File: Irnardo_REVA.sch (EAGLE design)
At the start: 21 parts, among them U1 ATMEGA32U4-MU, U2 TSOP755, X1 16MHz

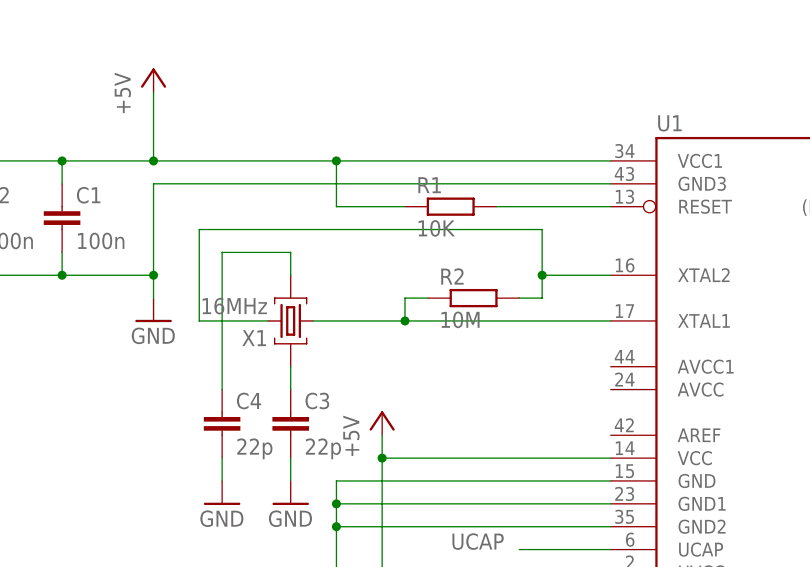
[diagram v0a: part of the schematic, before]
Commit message: Initial PCB design for DIY etching - incomplete
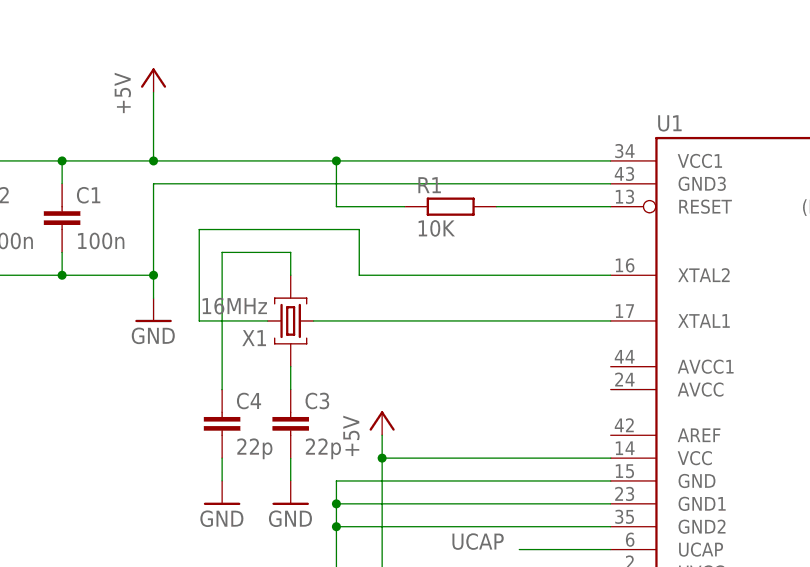
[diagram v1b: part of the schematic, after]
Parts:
- removed R2: 10M, resistor:R-EU_R0402
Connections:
- net N$1: no longer R2.1
- net N$2: no longer R2.2
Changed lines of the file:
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@@
 <?xml version="1.0" encoding="utf-8"?>
 <!DOCTYPE eagle SYSTEM "eagle.dtd">
-<eagle version="6.5.0">
+<eagle version="6.4">
 <drawing>
 <settings>
@@
 <part name="R1" library="resistor" deviceset="R-EU_" device="R0402" value="10K"/>
 <part name="C1" library="resistor" deviceset="C-EU" device="C0402" value="100n"/>
-<part name="R2" library="resistor" deviceset="R-EU_" device="R0402" value="10M"/>
 <part name="P+3" library="supply1" deviceset="+5V" device=""/>
 <part name="GND3" library="supply1" deviceset="GND" device=""/>
@@
 <instance part="R1" gate="G$1" x="58.42" y="101.6"/>
 <instance part="C1" gate="G$1" x="15.24" y="101.6"/>
-<instance part="R2" gate="G$1" x="60.96" y="91.44"/>
 <instance part="P+3" gate="1" x="50.8" y="78.74"/>
 <instance part="GND3" gate="1" x="45.72" y="55.88"/>
@@
 <pinref part="U1" gate="G$1" pin="XTAL1"/>
 <pinref part="X1" gate="G$1" pin="C1"/>
-<wire x1="76.2" y1="88.9" x2="53.34" y2="88.9" width="0.1524" layer="91"/>
-<pinref part="R2" gate="G$1" pin="1"/>
-<wire x1="53.34" y1="88.9" x2="43.18" y2="88.9" width="0.1524" layer="91"/>
-<wire x1="55.88" y1="91.44" x2="53.34" y2="91.44" width="0.1524" layer="91"/>
-<wire x1="53.34" y1="91.44" x2="53.34" y2="88.9" width="0.1524" layer="91"/>
-<junction x="53.34" y="88.9"/>
+<wire x1="76.2" y1="88.9" x2="43.18" y2="88.9" width="0.1524" layer="91"/>
 </segment>
 </net>
@@
 <segment>
 <pinref part="U1" gate="G$1" pin="XTAL2"/>
-<wire x1="76.2" y1="93.98" x2="68.58" y2="93.98" width="0.1524" layer="91"/>
-<wire x1="68.58" y1="93.98" x2="68.58" y2="99.06" width="0.1524" layer="91"/>
-<wire x1="68.58" y1="99.06" x2="30.48" y2="99.06" width="0.1524" layer="91"/>
+<wire x1="76.2" y1="93.98" x2="48.26" y2="93.98" width="0.1524" layer="91"/>
+<wire x1="48.26" y1="93.98" x2="48.26" y2="99.06" width="0.1524" layer="91"/>
+<wire x1="48.26" y1="99.06" x2="30.48" y2="99.06" width="0.1524" layer="91"/>
 <wire x1="30.48" y1="99.06" x2="30.48" y2="88.9" width="0.1524" layer="91"/>
 <pinref part="X1" gate="G$1" pin="C2"/>
 <wire x1="30.48" y1="88.9" x2="38.1" y2="88.9" width="0.1524" layer="91"/>
-<pinref part="R2" gate="G$1" pin="2"/>
-<wire x1="66.04" y1="91.44" x2="68.58" y2="91.44" width="0.1524" layer="91"/>
-<wire x1="68.58" y1="91.44" x2="68.58" y2="93.98" width="0.1524" layer="91"/>
-<junction x="68.58" y="93.98"/>
-</segment>
-</net>
+</segment>
+</net>

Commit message: Finished placing and stated wiring REVA
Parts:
- added J1: ICSP, 6X2005IN:6X2005IN
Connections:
- removed net N$3: R1.2, U1.RESET
- removed net N$4: C4.1, X1.GND@1
- removed net N$6: C3.1, X1.GND@2
- new net MISO: J1.1, U1.(PD0/MISO/PCINT3)PB3
- new net MOSI: J1.4, U1.(PDI/MOSI/PCINT2)PB2
- new net RESET: J1.5, R1.2, U1.RESET
- new net SCK: J1.3, U1.(SCLK/PCINT1)PB1
- net +5V: now also J1.2
- net GND: now also J1.6, X1.GND@1, X1.GND@2
- net N$1: now also C3.1
- net N$2: now also C4.1
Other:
- note added: "ICSP"
- note added: "REVA"
- note added: "© 2014 - Bracken Dawson"
- moved on the sheet: C3, C4, R1, X1
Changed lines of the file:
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@@
 <?xml version="1.0" encoding="utf-8"?>
 <!DOCTYPE eagle SYSTEM "eagle.dtd">
-<eagle version="6.4">
+<eagle version="6.5.0">
 <drawing>
 <settings>
@@
 <part name="C7" library="resistor" deviceset="C-EU" device="C0402" value="100n"/>
 <part name="GND12" library="supply1" deviceset="GND" device=""/>
+<part name="P+5" library="supply1" deviceset="+5V" device=""/>
+<part name="GND13" library="supply1" deviceset="GND" device=""/>
+<part name="J1" library="6X2005IN" deviceset="6X2005IN" device="" value="ICSP"/>
 </parts>
 <sheets>
@@
 <frame x1="-48.26" y1="-20.32" x2="256.54" y2="172.72" columns="8" rows="5" layer="91"/>
 <text x="155.194" y="74.93" size="1.778" layer="97">USB Boot En</text>
+<text x="-33.02" y="132.08" size="5.08" layer="91">REVA</text>
+<text x="167.64" y="-12.7" size="5.08" layer="91">© 2014 - Bracken Dawson</text>
+<text x="175.26" y="40.64" size="5.08" layer="91">ICSP</text>
 </plain>
 <instances>
@@
 <instance part="P+1" gate="1" x="25.4" y="116.84"/>
 <instance part="GND1" gate="1" x="25.4" y="88.9"/>
-<instance part="R1" gate="G$1" x="58.42" y="101.6"/>
+<instance part="R1" gate="G$1" x="58.42" y="109.22"/>
 <instance part="C1" gate="G$1" x="15.24" y="101.6"/>
 <instance part="P+3" gate="1" x="50.8" y="78.74"/>
 <instance part="GND3" gate="1" x="45.72" y="55.88"/>
 <instance part="GND4" gate="1" x="68.58" y="25.4"/>
-<instance part="X1" gate="G$1" x="40.64" y="88.9" rot="R180"/>
-<instance part="C3" gate="G$1" x="40.64" y="78.74"/>
-<instance part="C4" gate="G$1" x="33.02" y="78.74"/>
-<instance part="GND2" gate="1" x="40.64" y="68.58"/>
+<instance part="X1" gate="G$1" x="35.56" y="88.9" rot="R180"/>
+<instance part="C3" gate="G$1" x="40.64" y="83.82"/>
+<instance part="C4" gate="G$1" x="30.48" y="83.82"/>
+<instance part="GND2" gate="1" x="40.64" y="71.12"/>
 <instance part="C2" gate="G$1" x="5.08" y="101.6"/>
-<instance part="GND5" gate="1" x="33.02" y="68.58"/>
+<instance part="GND5" gate="1" x="30.48" y="71.12"/>
 <instance part="R3" gate="G$1" x="-12.7" y="45.72"/>
 <instance part="R4" gate="G$1" x="-12.7" y="38.1"/>
@@
 <instance part="C7" gate="G$1" x="10.16" y="53.34" rot="R90"/>
 <instance part="GND12" gate="1" x="22.86" y="53.34" rot="R90"/>
+<instance part="P+5" gate="1" x="215.9" y="38.1"/>
+<instance part="GND13" gate="1" x="215.9" y="12.7"/>
+<instance part="J1" gate="G$1" x="195.58" y="25.4"/>
 </instances>
 <busses>
@@
 <junction x="25.4" y="106.68"/>
 <pinref part="R1" gate="G$1" pin="1"/>
-<wire x1="53.34" y1="101.6" x2="45.72" y2="101.6" width="0.1524" layer="91"/>
-<wire x1="45.72" y1="101.6" x2="45.72" y2="106.68" width="0.1524" layer="91"/>
+<wire x1="53.34" y1="109.22" x2="45.72" y2="109.22" width="0.1524" layer="91"/>
+<wire x1="45.72" y1="109.22" x2="45.72" y2="106.68" width="0.1524" layer="91"/>
 <junction x="45.72" y="106.68"/>
 <pinref part="C2" gate="G$1" pin="1"/>
@@
 <wire x1="182.88" y1="93.98" x2="182.88" y2="96.52" width="0.1524" layer="91"/>
 <junction x="182.88" y="96.52"/>
+</segment>
+<segment>
+<pinref part="P+5" gate="1" pin="+5V"/>
+<wire x1="205.74" y1="27.94" x2="215.9" y2="27.94" width="0.1524" layer="91"/>
+<wire x1="215.9" y1="27.94" x2="215.9" y2="35.56" width="0.1524" layer="91"/>
+<pinref part="J1" gate="G$1" pin="2"/>
 </segment>
 </net>
@@
 <pinref part="GND2" gate="1" pin="GND"/>
 <pinref part="C3" gate="G$1" pin="2"/>
-<wire x1="40.64" y1="73.66" x2="40.64" y2="71.12" width="0.1524" layer="91"/>
+<wire x1="40.64" y1="78.74" x2="40.64" y2="76.2" width="0.1524" layer="91"/>
+<pinref part="X1" gate="G$1" pin="GND@2"/>
+<wire x1="40.64" y1="76.2" x2="40.64" y2="73.66" width="0.1524" layer="91"/>
+<wire x1="35.56" y1="83.82" x2="35.56" y2="76.2" width="0.1524" layer="91"/>
+<wire x1="35.56" y1="76.2" x2="40.64" y2="76.2" width="0.1524" layer="91"/>
+<wire x1="40.64" y1="76.2" x2="45.72" y2="76.2" width="0.1524" layer="91"/>
+<wire x1="45.72" y1="76.2" x2="45.72" y2="96.52" width="0.1524" layer="91"/>
+<wire x1="45.72" y1="96.52" x2="35.56" y2="96.52" width="0.1524" layer="91"/>
+<pinref part="X1" gate="G$1" pin="GND@1"/>
+<wire x1="35.56" y1="96.52" x2="35.56" y2="93.98" width="0.1524" layer="91"/>
+<junction x="40.64" y="76.2"/>
 </segment>
 <segment>
 <pinref part="C4" gate="G$1" pin="2"/>
-<wire x1="33.02" y1="73.66" x2="33.02" y2="71.12" width="0.1524" layer="91"/>
+<wire x1="30.48" y1="78.74" x2="30.48" y2="73.66" width="0.1524" layer="91"/>
 <pinref part="GND5" gate="1" pin="GND"/>
 </segment>
@@
 <wire x1="15.24" y1="53.34" x2="20.32" y2="53.34" width="0.1524" layer="91"/>
 </segment>
-</net>
-<net name="N$3" class="0">
+<segment>
+<wire x1="205.74" y1="22.86" x2="215.9" y2="22.86" width="0.1524" layer="91"/>
+<pinref part="GND13" gate="1" pin="GND"/>
+<wire x1="215.9" y1="22.86" x2="215.9" y2="15.24" width="0.1524" layer="91"/>
+<pinref part="J1" gate="G$1" pin="6"/>
+</segment>
+</net>
+<net name="RESET" class="0">
 <segment>
 <pinref part="U1" gate="G$1" pin="RESET"/>
 <pinref part="R1" gate="G$1" pin="2"/>
-<wire x1="76.2" y1="101.6" x2="63.5" y2="101.6" width="0.1524" layer="91"/>
+<wire x1="76.2" y1="101.6" x2="71.12" y2="101.6" width="0.1524" layer="91"/>
+<wire x1="71.12" y1="101.6" x2="71.12" y2="109.22" width="0.1524" layer="91"/>
+<wire x1="71.12" y1="109.22" x2="63.5" y2="109.22" width="0.1524" layer="91"/>
+<wire x1="71.12" y1="101.6" x2="66.04" y2="101.6" width="0.1524" layer="91"/>
+<junction x="71.12" y="101.6"/>
+<label x="55.88" y="101.6" size="1.778" layer="95"/>
+</segment>
+<segment>
+<wire x1="185.42" y1="22.86" x2="175.26" y2="22.86" width="0.1524" layer="91"/>
+<label x="165.1" y="22.86" size="1.778" layer="95"/>
+<pinref part="J1" gate="G$1" pin="5"/>
 </segment>
 </net>
@@
 <pinref part="U1" gate="G$1" pin="XTAL1"/>
 <pinref part="X1" gate="G$1" pin="C1"/>
-<wire x1="76.2" y1="88.9" x2="43.18" y2="88.9" width="0.1524" layer="91"/>
+<wire x1="76.2" y1="88.9" x2="40.64" y2="88.9" width="0.1524" layer="91"/>
+<pinref part="C3" gate="G$1" pin="1"/>
+<wire x1="40.64" y1="88.9" x2="38.1" y2="88.9" width="0.1524" layer="91"/>
+<wire x1="40.64" y1="86.36" x2="40.64" y2="88.9" width="0.1524" layer="91"/>
+<junction x="40.64" y="88.9"/>
 </segment>
 </net>
@@
 <wire x1="30.48" y1="99.06" x2="30.48" y2="88.9" width="0.1524" layer="91"/>
 <pinref part="X1" gate="G$1" pin="C2"/>
-<wire x1="30.48" y1="88.9" x2="38.1" y2="88.9" width="0.1524" layer="91"/>
-</segment>
-</net>
-<net name="N$4" class="0">
-<segment>
-<pinref part="X1" gate="G$1" pin="GND@1"/>
-<wire x1="40.64" y1="93.98" x2="40.64" y2="96.52" width="0.1524" layer="91"/>
-<wire x1="40.64" y1="96.52" x2="33.02" y2="96.52" width="0.1524" layer="91"/>
 <pinref part="C4" gate="G$1" pin="1"/>
-<wire x1="33.02" y1="96.52" x2="33.02" y2="81.28" width="0.1524" layer="91"/>
-</segment>
-</net>
-<net name="N$6" class="0">
-<segment>
-<pinref part="C3" gate="G$1" pin="1"/>
-<pinref part="X1" gate="G$1" pin="GND@2"/>
-<wire x1="40.64" y1="81.28" x2="40.64" y2="83.82" width="0.1524" layer="91"/>
+<wire x1="30.48" y1="88.9" x2="33.02" y2="88.9" width="0.1524" layer="91"/>
+<wire x1="30.48" y1="86.36" x2="30.48" y2="88.9" width="0.1524" layer="91"/>
+<junction x="30.48" y="88.9"/>
 </segment>
 </net>
@@
 </segment>
 </net>
+<net name="MISO" class="0">
+<segment>
+<pinref part="U1" gate="G$1" pin="(PD0/MISO/PCINT3)PB3"/>
+<wire x1="137.16" y1="96.52" x2="147.32" y2="96.52" width="0.1524" layer="91"/>
+<label x="147.32" y="96.52" size="1.778" layer="95"/>
+</segment>
+<segment>
+<wire x1="185.42" y1="27.94" x2="175.26" y2="27.94" width="0.1524" layer="91"/>
+<label x="167.64" y="27.94" size="1.778" layer="95"/>
+<pinref part="J1" gate="G$1" pin="1"/>
+</segment>
+</net>
+<net name="SCK" class="0">
+<segment>
+<pinref part="U1" gate="G$1" pin="(SCLK/PCINT1)PB1"/>
+<wire x1="137.16" y1="91.44" x2="147.32" y2="91.44" width="0.1524" layer="91"/>
+<label x="147.32" y="91.44" size="1.778" layer="95"/>
+</segment>
+<segment>
+<wire x1="185.42" y1="25.4" x2="175.26" y2="25.4" width="0.1524" layer="91"/>
+<label x="167.64" y="25.4" size="1.778" layer="95"/>
+<pinref part="J1" gate="G$1" pin="3"/>
+</segment>
+</net>
+<net name="MOSI" class="0">
+<segment>
+<pinref part="U1" gate="G$1" pin="(PDI/MOSI/PCINT2)PB2"/>
+<wire x1="137.16" y1="93.98" x2="147.32" y2="93.98" width="0.1524" layer="91"/>
+<label x="147.32" y="93.98" size="1.778" layer="95"/>
+</segment>
+<segment>
+<wire x1="205.74" y1="25.4" x2="215.9" y2="25.4" width="0.1524" layer="91"/>
+<label x="215.9" y="25.4" size="1.778" layer="95"/>
+<pinref part="J1" gate="G$1" pin="4"/>
+</segment>
+</net>

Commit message: First complete(ish) layout.
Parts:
- removed R8: 10K, resistor:R-EU_R0402
- J1: value ICSP -> USB_PAD; device 6X2005IN:6X2005IN -> USB_PAD:USB_PAD
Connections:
- removed net N$9: R8.1, U1.(#HWB)PE2
- net +5V: now also J1.V+; no longer J1.2
- net D+: now also J1.D+
- net D-: now also J1.D-
- net GND: now also U1.(#HWB)PE2; no longer J1.6, R8.2
- net MISO: no longer J1.1
- net MOSI: no longer J1.4
- net RESET: no longer J1.5
- net SCK: no longer J1.3
- net UGND: now also J1.V-
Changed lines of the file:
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@@
 <part name="D2" library="led" deviceset="LED" device="SML0603" value="950nm"/>
 <part name="GND10" library="supply1" deviceset="GND" device=""/>
-<part name="R8" library="resistor" deviceset="R-EU_" device="R0402" value="10K"/>
 <part name="GND11" library="supply1" deviceset="GND" device=""/>
 <part name="C7" library="resistor" deviceset="C-EU" device="C0402" value="100n"/>
@@
 <part name="P+5" library="supply1" deviceset="+5V" device=""/>
 <part name="GND13" library="supply1" deviceset="GND" device=""/>
-<part name="J1" library="6X2005IN" deviceset="6X2005IN" device="" value="ICSP"/>
+<part name="J1" library="USB_PAD" deviceset="USB_PAD" device=""/>
 </parts>
 <sheets>
@@
 <instance part="D2" gate="G$1" x="213.36" y="60.96" rot="R90"/>
 <instance part="GND10" gate="1" x="231.14" y="60.96" rot="R90"/>
-<instance part="R8" gate="G$1" x="160.02" y="71.12"/>
 <instance part="GND11" gate="1" x="170.18" y="71.12" rot="R90"/>
 <instance part="C7" gate="G$1" x="10.16" y="53.34" rot="R90"/>
@@
 <instance part="P+5" gate="1" x="215.9" y="38.1"/>
 <instance part="GND13" gate="1" x="215.9" y="12.7"/>
-<instance part="J1" gate="G$1" x="195.58" y="25.4"/>
+<instance part="J1" gate="G$1" x="-33.02" y="43.18"/>
 </instances>
 <busses>
@@
 <pinref part="P+2" gate="1" pin="+5V"/>
 <wire x1="2.54" y1="55.88" x2="2.54" y2="53.34" width="0.1524" layer="91"/>
-<wire x1="2.54" y1="53.34" x2="-27.94" y2="53.34" width="0.1524" layer="91"/>
-<label x="-27.94" y="53.34" size="1.778" layer="95" rot="R180" xref="yes"/>
+<wire x1="2.54" y1="53.34" x2="-20.32" y2="53.34" width="0.1524" layer="91"/>
 <pinref part="C7" gate="G$1" pin="1"/>
 <wire x1="2.54" y1="53.34" x2="7.62" y2="53.34" width="0.1524" layer="91"/>
 <junction x="2.54" y="53.34"/>
+<pinref part="J1" gate="G$1" pin="V+"/>
 </segment>
 <segment>
@@
 <segment>
 <pinref part="P+5" gate="1" pin="+5V"/>
-<wire x1="205.74" y1="27.94" x2="215.9" y2="27.94" width="0.1524" layer="91"/>
+<wire x1="203.2" y1="27.94" x2="215.9" y2="27.94" width="0.1524" layer="91"/>
 <wire x1="215.9" y1="27.94" x2="215.9" y2="35.56" width="0.1524" layer="91"/>
-<pinref part="J1" gate="G$1" pin="2"/>
 </segment>
 </net>
@@
 </segment>
 <segment>
-<pinref part="R8" gate="G$1" pin="2"/>
 <pinref part="GND11" gate="1" pin="GND"/>
-<wire x1="165.1" y1="71.12" x2="167.64" y2="71.12" width="0.1524" layer="91"/>
+<pinref part="U1" gate="G$1" pin="(#HWB)PE2"/>
+<wire x1="137.16" y1="71.12" x2="167.64" y2="71.12" width="0.1524" layer="91"/>
 </segment>
 <segment>
@@
 </segment>
 <segment>
-<wire x1="205.74" y1="22.86" x2="215.9" y2="22.86" width="0.1524" layer="91"/>
+<wire x1="203.2" y1="22.86" x2="215.9" y2="22.86" width="0.1524" layer="91"/>
 <pinref part="GND13" gate="1" pin="GND"/>
 <wire x1="215.9" y1="22.86" x2="215.9" y2="15.24" width="0.1524" layer="91"/>
-<pinref part="J1" gate="G$1" pin="6"/>
 </segment>
 </net>
@@
 <wire x1="185.42" y1="22.86" x2="175.26" y2="22.86" width="0.1524" layer="91"/>
 <label x="165.1" y="22.86" size="1.778" layer="95"/>
-<pinref part="J1" gate="G$1" pin="5"/>
 </segment>
 </net>
@@
 <pinref part="L1" gate="G$1" pin="1"/>
 <wire x1="-12.7" y1="27.94" x2="-12.7" y2="30.48" width="0.1524" layer="91"/>
-<wire x1="-12.7" y1="30.48" x2="-27.94" y2="30.48" width="0.1524" layer="91"/>
-<label x="-27.94" y="30.48" size="1.778" layer="95" rot="R180" xref="yes"/>
+<wire x1="-12.7" y1="30.48" x2="-20.32" y2="30.48" width="0.1524" layer="91"/>
 <label x="2.54" y="30.48" size="1.778" layer="95"/>
 <wire x1="-12.7" y1="30.48" x2="-5.08" y2="30.48" width="0.1524" layer="91"/>
@@
 <junction x="-12.7" y="30.48"/>
 <junction x="-5.08" y="30.48"/>
+<pinref part="J1" gate="G$1" pin="V-"/>
 </segment>
 </net>
@@
 <segment>
 <pinref part="R4" gate="G$1" pin="1"/>
-<wire x1="-17.78" y1="38.1" x2="-25.4" y2="38.1" width="0.1524" layer="91"/>
-<label x="-25.4" y="38.1" size="1.778" layer="95" rot="R180" xref="yes"/>
+<wire x1="-17.78" y1="38.1" x2="-22.86" y2="38.1" width="0.1524" layer="91"/>
+<pinref part="J1" gate="G$1" pin="D+"/>
 </segment>
 </net>
@@
 <segment>
 <pinref part="R3" gate="G$1" pin="1"/>
-<wire x1="-17.78" y1="45.72" x2="-25.4" y2="45.72" width="0.1524" layer="91"/>
-<label x="-25.4" y="45.72" size="1.778" layer="95" rot="R180" xref="yes"/>
+<wire x1="-17.78" y1="45.72" x2="-22.86" y2="45.72" width="0.1524" layer="91"/>
+<pinref part="J1" gate="G$1" pin="D-"/>
 </segment>
 </net>
@@
 </segment>
 </net>
-<net name="N$9" class="0">
-<segment>
-<pinref part="U1" gate="G$1" pin="(#HWB)PE2"/>
-<pinref part="R8" gate="G$1" pin="1"/>
-<wire x1="137.16" y1="71.12" x2="154.94" y2="71.12" width="0.1524" layer="91"/>
-</segment>
-</net>
 <net name="MISO" class="0">
 <segment>
@@
 <wire x1="185.42" y1="27.94" x2="175.26" y2="27.94" width="0.1524" layer="91"/>
 <label x="167.64" y="27.94" size="1.778" layer="95"/>
-<pinref part="J1" gate="G$1" pin="1"/>
 </segment>
 </net>
@@
 <wire x1="185.42" y1="25.4" x2="175.26" y2="25.4" width="0.1524" layer="91"/>
 <label x="167.64" y="25.4" size="1.778" layer="95"/>
-<pinref part="J1" gate="G$1" pin="3"/>
 </segment>
 </net>
@@
 </segment>
 <segment>
-<wire x1="205.74" y1="25.4" x2="215.9" y2="25.4" width="0.1524" layer="91"/>
+<wire x1="203.2" y1="25.4" x2="215.9" y2="25.4" width="0.1524" layer="91"/>
 <label x="215.9" y="25.4" size="1.778" layer="95"/>
-<pinref part="J1" gate="G$1" pin="4"/>
-</segment>
-</net>
+</segment>
+</net>

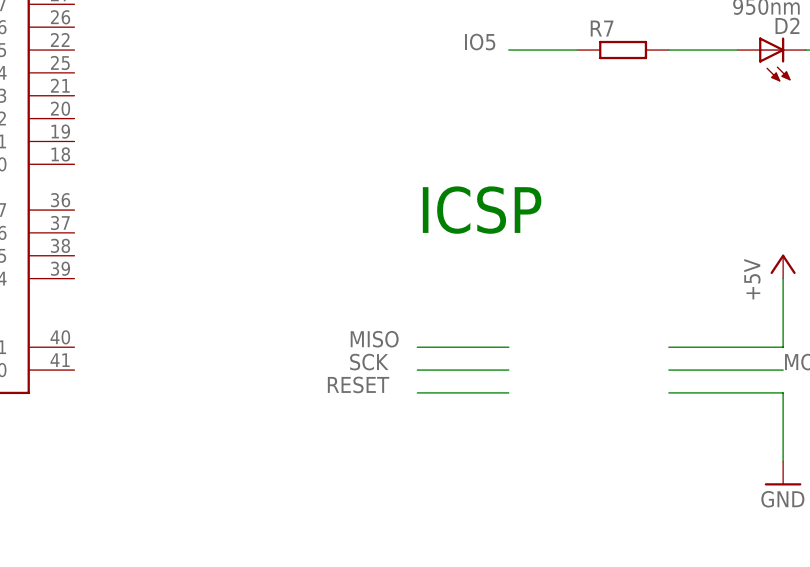
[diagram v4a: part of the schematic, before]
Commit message: Fixes at hackerspace after printing and talking to
Joel.
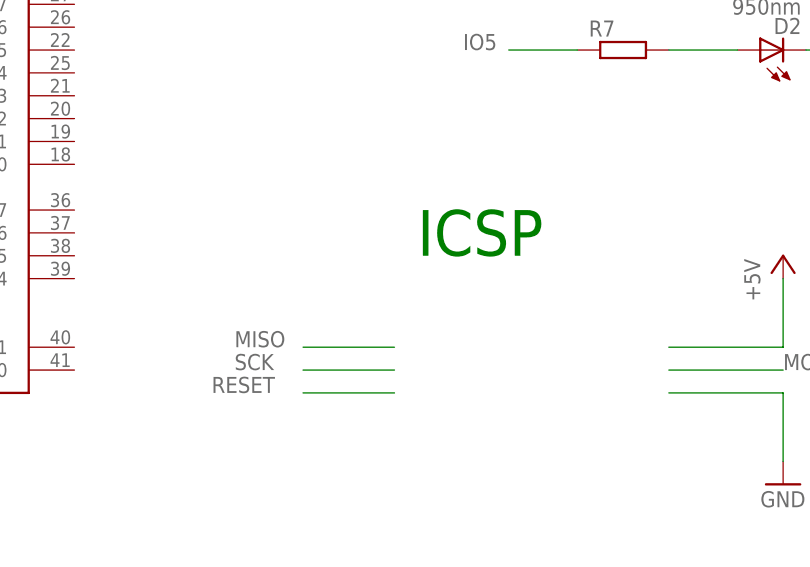
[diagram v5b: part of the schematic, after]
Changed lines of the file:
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@@
 <text x="-33.02" y="132.08" size="5.08" layer="91">REVA</text>
 <text x="167.64" y="-12.7" size="5.08" layer="91">© 2014 - Bracken Dawson</text>
-<text x="175.26" y="40.64" size="5.08" layer="91">ICSP</text>
+<text x="175.26" y="38.1" size="5.08" layer="91">ICSP</text>
 </plain>
 <instances>
@@
 </segment>
 <segment>
-<wire x1="185.42" y1="22.86" x2="175.26" y2="22.86" width="0.1524" layer="91"/>
-<label x="165.1" y="22.86" size="1.778" layer="95"/>
+<wire x1="172.72" y1="22.86" x2="162.56" y2="22.86" width="0.1524" layer="91"/>
+<label x="152.4" y="22.86" size="1.778" layer="95"/>
 </segment>
 </net>
@@
 </segment>
 <segment>
-<wire x1="185.42" y1="27.94" x2="175.26" y2="27.94" width="0.1524" layer="91"/>
-<label x="167.64" y="27.94" size="1.778" layer="95"/>
+<wire x1="172.72" y1="27.94" x2="162.56" y2="27.94" width="0.1524" layer="91"/>
+<label x="154.94" y="27.94" size="1.778" layer="95"/>
 </segment>
 </net>
@@
 </segment>
 <segment>
-<wire x1="185.42" y1="25.4" x2="175.26" y2="25.4" width="0.1524" layer="91"/>
-<label x="167.64" y="25.4" size="1.778" layer="95"/>
-</segment>
-</net>
+<wire x1="172.72" y1="25.4" x2="162.56" y2="25.4" width="0.1524" layer="91"/>
+<label x="154.94" y="25.4" size="1.778" layer="95"/>
+</segment>
+</net>
